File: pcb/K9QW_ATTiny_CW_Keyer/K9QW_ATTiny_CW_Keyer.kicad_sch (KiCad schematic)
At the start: 30 parts, among them J1 Paddle Input, J2 Key Output, J3 Command, J4 Sidetone, J5 Barrel_Jack_MountingPin, J6 Paddle Input, J7 Key Output, J8 LED, J9 Power Input, Q1 MMBT2222A, Q2 MMBT3904, Q3 MMBT3904, SW1 Command, SW2 Power Switch, U1 ATtiny85-20P, U2 LD1117S33TR_SOT223

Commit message: Rough PCB Layout
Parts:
- D1: value LED -> Key
- D2: value Side LED -> Sidetone
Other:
- moved on the sheet: R6
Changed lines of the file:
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@@
 	(wire
 		(pts
-			(xy 203.2 125.73) (xy 203.2 135.89)
+			(xy 205.74 125.73) (xy 205.74 135.89)
 		)
 		(stroke
@@
 	(wire
 		(pts
-			(xy 203.2 135.89) (xy 193.04 135.89)
+			(xy 205.74 135.89) (xy 193.04 135.89)
 		)
 		(stroke
@@
 	(wire
 		(pts
-			(xy 210.82 137.16) (xy 212.09 137.16)
+			(xy 212.09 137.16) (xy 214.63 137.16)
 		)
 		(stroke
@@
 	(wire
 		(pts
-			(xy 245.11 125.73) (xy 203.2 125.73)
+			(xy 245.11 125.73) (xy 205.74 125.73)
 		)
 		(stroke
@@
 	(wire
 		(pts
-			(xy 219.71 137.16) (xy 223.52 137.16)
+			(xy 222.25 137.16) (xy 223.52 137.16)
 		)
 		(stroke
@@
 			)
 		)
-		(property "Value" "LED"
+		(property "Value" "Key"
 			(at 196.85 132.3974 90)
 			(effects
@@
 	(symbol
 		(lib_id "power:VCC")
-		(at 210.82 137.16 90)
+		(at 212.09 137.16 90)
 		(unit 1)
 		(exclude_from_sim no)
@@
 		(dnp no)
 		(property "Reference" "#PWR020"
-			(at 214.63 137.16 0)
+			(at 215.9 137.16 0)
 			(effects
 				(font
@@
 		)
 		(property "Value" "VCC"
-			(at 205.74 137.16 0)
+			(at 207.01 137.16 0)
 			(effects
 				(font
@@
 		)
 		(property "Footprint" ""
-			(at 210.82 137.16 0)
+			(at 212.09 137.16 0)
 			(effects
 				(font
@@
 		)
 		(property "Datasheet" ""
-			(at 210.82 137.16 0)
+			(at 212.09 137.16 0)
 			(effects
 				(font
@@
 		)
 		(property "Description" "Power symbol creates a global label with name \"VCC\""
-			(at 210.82 137.16 0)
+			(at 212.09 137.16 0)
 			(effects
 				(font
@@
 			)
 		)
-		(property "Value" "Side LED"
+		(property "Value" "Sidetone"
 			(at 231.4575 133.35 0)
 			(effects
@@
 	(symbol
 		(lib_id "Device:R")
-		(at 215.9 137.16 270)
+		(at 218.44 137.16 270)
 		(unit 1)
 		(exclude_from_sim no)
@@
 		(fields_autoplaced yes)
 		(property "Reference" "R6"
-			(at 215.9 130.81 90)
+			(at 218.44 130.81 90)
 			(effects
 				(font
@@
 		)
 		(property "Value" "220"
-			(at 215.9 133.35 90)
+			(at 218.44 133.35 90)
 			(effects
 				(font
@@
 		)
 		(property "Footprint" "Resistor_SMD:R_0603_1608Metric_Pad0.98x0.95mm_HandSolder"
-			(at 215.9 135.382 90)
+			(at 218.44 135.382 90)
 			(effects
 				(font
@@
 		)
 		(property "Datasheet" "~"
-			(at 215.9 137.16 0)
+			(at 218.44 137.16 0)
 			(effects
 				(font
@@
 		)
 		(property "Description" "Resistor"
-			(at 215.9 137.16 0)
+			(at 218.44 137.16 0)
 			(effects
 				(font

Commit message: Layout cleanup
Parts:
- added JP1: SolderJumper_2_Open, Jumper:SolderJumper-2_P1.3mm_Open_RoundedPad1.0x1.5mm, symbol Jumper:SolderJumper_2_Open
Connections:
- net VCC: now also JP1.2 (B)
- net at C5.1, SW2.2 (B), U2.3 (VI): now also JP1.1 (A)
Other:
- moved on the sheet: C5, C6, SW2, U2

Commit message: Refining layout
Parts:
- added R7: 50, Resistor_SMD:R_0603_1608Metric_Pad0.98x0.95mm_HandSolder, symbol Device:R
- SW2: footprint Button_Switch_THT:SW_Slide-03_Wuerth-WS-SLTV_10x2.5x6.4_P2.54mm -> Connector_JST:JST_XH_B3B-XH-A_1x03_P2.50mm_Vertical
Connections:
- net DAH: now also J6.1 (Pin_1); no longer J6.2 (Pin_2)
- net DIT: now also J6.2 (Pin_2); no longer J6.3 (Pin_3)
- net GND: now also J6.3 (Pin_3), J7.3 (Pin_3), R7.2; no longer J6.1 (Pin_1), J7.1 (Pin_1), SW2.1 (A)
- net KEY Out: now also J7.2 (Pin_2); no longer J7.3 (Pin_3)
- net KEY Ring: now also J7.1 (Pin_1); no longer J7.2 (Pin_2)
- new net: R7.1, SW2.1 (A)
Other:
- moved on the sheet: J6, J7
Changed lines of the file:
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@@
 	(wire
 		(pts
-			(xy 240.03 24.13) (xy 242.57 24.13)
+			(xy 240.03 31.75) (xy 242.57 31.75)
 		)
 		(stroke
@@
 	(wire
 		(pts
+			(xy 54.61 86.36) (xy 55.88 86.36)
+		)
+		(stroke
+			(width 0)
+			(type default)
+		)
+	)
+	(wire
+		(pts
 			(xy 210.82 24.13) (xy 213.36 24.13)
 		)
@@
 	(wire
 		(pts
-			(xy 241.3 52.07) (xy 242.57 52.07)
+			(xy 241.3 59.69) (xy 242.57 59.69)
 		)
 		(stroke
@@
 	(wire
 		(pts
-			(xy 105.41 156.21) (xy 127 156.21)
+			(xy 63.5 86.36) (xy 64.77 86.36)
 		)
 		(stroke
@@
 	(wire
 		(pts
-			(xy 105.41 148.59) (xy 109.22 148.59)
+			(xy 105.41 156.21) (xy 127 156.21)
 		)
 		(stroke
@@
 	(wire
 		(pts
-			(xy 127 142.24) (xy 127 134.62)
+			(xy 105.41 148.59) (xy 109.22 148.59)
 		)
 		(stroke
@@
 	(wire
 		(pts
-			(xy 105.41 78.74) (xy 114.3 78.74)
+			(xy 127 142.24) (xy 127 134.62)
 		)
 		(stroke
@@
 	(wire
 		(pts
-			(xy 60.96 86.36) (xy 64.77 86.36)
+			(xy 105.41 78.74) (xy 114.3 78.74)
 		)
 		(stroke
@@
 		(on_board yes)
 		(dnp no)
-		(fields_autoplaced yes)
 		(property "Reference" "J3"
 			(at 232.41 81.2799 0)
@@
 	(symbol
 		(lib_id "Connector_Generic:Conn_01x03")
-		(at 247.65 54.61 0)
+		(at 247.65 57.15 0)
 		(unit 1)
 		(exclude_from_sim no)
@@
 		(fields_autoplaced yes)
 		(property "Reference" "J7"
-			(at 250.19 53.3399 0)
+			(at 250.19 55.8799 0)
 			(effects
 				(font
@@
 		)
 		(property "Value" "Key Output"
-			(at 250.19 55.8799 0)
+			(at 250.19 58.4199 0)
 			(effects
 				(font
@@
 		)
 		(property "Footprint" "Connector_JST:JST_XH_B3B-XH-A_1x03_P2.50mm_Vertical"
-			(at 247.65 54.61 0)
+			(at 247.65 57.15 0)
 			(effects
 				(font
@@
 		)
 		(property "Datasheet" "~"
-			(at 247.65 54.61 0)
+			(at 247.65 57.15 0)
 			(effects
 				(font
@@
 		)
 		(property "Description" "Generic connector, single row, 01x03, script generated (kicad-library-utils/schlib/autogen/connector/)"
-			(at 247.65 54.61 0)
+			(at 247.65 57.15 0)
 			(effects
 				(font
@@
 	(symbol
 		(lib_id "Connector_Generic:Conn_01x03")
-		(at 247.65 26.67 0)
+		(at 247.65 29.21 0)
 		(unit 1)
 		(exclude_from_sim no)
@@
 		(fields_autoplaced yes)
 		(property "Reference" "J6"
-			(at 250.19 25.3999 0)
+			(at 250.19 27.9399 0)
 			(effects
 				(font
@@
 		)
 		(property "Value" "Paddle Input"
-			(at 250.19 27.9399 0)
+			(at 250.19 30.4799 0)
 			(effects
 				(font
@@
 		)
 		(property "Footprint" "Connector_JST:JST_XH_B3B-XH-A_1x03_P2.50mm_Vertical"
-			(at 247.65 26.67 0)
+			(at 247.65 29.21 0)
 			(effects
 				(font
@@
 		)
 		(property "Datasheet" "~"
-			(at 247.65 26.67 0)
+			(at 247.65 29.21 0)
 			(effects
 				(font
@@
 		)
 		(property "Description" "Generic connector, single row, 01x03, script generated (kicad-library-utils/schlib/autogen/connector/)"
-			(at 247.65 26.67 0)
+			(at 247.65 29.21 0)
 			(effects
 				(font
@@
 	(symbol
 		(lib_id "power:GND")
-		(at 60.96 86.36 270)
+		(at 54.61 86.36 270)
 		(unit 1)
 		(exclude_from_sim no)
@@
 		(fields_autoplaced yes)
 		(property "Reference" "#PWR016"
-			(at 54.61 86.36 0)
+			(at 48.26 86.36 0)
 			(effects
 				(font
@@
 		)
 		(property "Value" "GND"
-			(at 57.15 86.3599 90)
+			(at 50.8 86.3599 90)
 			(effects
 				(font
@@
 		)
 		(property "Footprint" ""
-			(at 60.96 86.36 0)
+			(at 54.61 86.36 0)
 			(effects
 				(font
@@
 		)
 		(property "Datasheet" ""
-			(at 60.96 86.36 0)
+			(at 54.61 86.36 0)
 			(effects
 				(font
@@
 		)
 		(property "Description" "Power symbol creates a global label with name \"GND\" , ground"
-			(at 60.96 86.36 0)
+			(at 54.61 86.36 0)
 			(effects
 				(font
@@
 			)
 		)
-		(property "Footprint" "Button_Switch_THT:SW_Slide-03_Wuerth-WS-SLTV_10x2.5x6.4_P2.54mm"
+		(property "Footprint" "Connector_JST:JST_XH_B3B-XH-A_1x03_P2.50mm_Vertical"
 			(at 69.85 88.9 0)
 			(effects
@@
 	(symbol
 		(lib_id "power:GND")
-		(at 240.03 24.13 270)
+		(at 240.03 31.75 270)
 		(unit 1)
 		(exclude_from_sim no)
@@
 		(fields_autoplaced yes)
 		(property "Reference" "#PWR017"
-			(at 233.68 24.13 0)
+			(at 233.68 31.75 0)
 			(effects
 				(font
@@
 		)
 		(property "Value" "GND"
-			(at 236.22 24.1299 90)
+			(at 236.22 31.7499 90)
 			(effects
 				(font
@@
 		)
 		(property "Footprint" ""
-			(at 240.03 24.13 0)
+			(at 240.03 31.75 0)
 			(effects
 				(font
@@
 		)
 		(property "Datasheet" ""
-			(at 240.03 24.13 0)
+			(at 240.03 31.75 0)
 			(effects
 				(font
@@
 		)
 		(property "Description" "Power symbol creates a global label with name \"GND\" , ground"
-			(at 240.03 24.13 0)
+			(at 240.03 31.75 0)
 			(effects
 				(font
@@
 	(symbol
 		(lib_id "power:GND")
-		(at 241.3 52.07 270)
+		(at 241.3 59.69 270)
 		(unit 1)
 		(exclude_from_sim no)
@@
 		(fields_autoplaced yes)
 		(property "Reference" "#PWR018"
-			(at 234.95 52.07 0)
+			(at 234.95 59.69 0)
 			(effects
 				(font
@@
 		)
 		(property "Value" "GND"
-			(at 237.49 52.0699 90)
+			(at 237.49 59.6899 90)
 			(effects
 				(font
@@
 		)
 		(property "Footprint" ""
-			(at 241.3 52.07 0)
+			(at 241.3 59.69 0)
 			(effects
 				(font
@@
 		)
 		(property "Datasheet" ""
-			(at 241.3 52.07 0)
+			(at 241.3 59.69 0)
 			(effects
 				(font
@@
 		)
 		(property "Description" "Power symbol creates a global label with name \"GND\" , ground"
-			(at 241.3 52.07 0)
+			(at 241.3 59.69 0)
 			(effects
 				(font
@@
 	)
 	(symbol
+		(lib_id "Device:R")
+		(at 59.69 86.36 270)
+		(unit 1)
+		(exclude_from_sim no)
+		(in_bom yes)
+		(on_board yes)
+		(dnp no)
+		(fields_autoplaced yes)
+		(property "Reference" "R7"
+			(at 59.69 80.01 90)
+			(effects
+				(font
+					(size 1.27 1.27)
+				)
+			)
+		)
+		(property "Value" "50"
+			(at 59.69 82.55 90)
+			(effects
+				(font
+					(size 1.27 1.27)
+				)
+			)
+		)
+		(property "Footprint" "Resistor_SMD:R_0603_1608Metric_Pad0.98x0.95mm_HandSolder"
+			(at 59.69 84.582 90)
+			(effects
+				(font
+					(size 1.27 1.27)
+				)
+				(hide yes)
+			)
+		)
+		(property "Datasheet" "~"
+			(at 59.69 86.36 0)
+			(effects
+				(font
+					(size 1.27 1.27)
+				)
+				(hide yes)
+			)
+		)
+		(property "Description" "Resistor"
+			(at 59.69 86.36 0)
+			(effects
+				(font
+					(size 1.27 1.27)
+				)
+				(hide yes)
+			)
+		)
+		(pin "1"
+		)
+		(pin "2"
+		)
+		(instances
+			(project "K9QW_ATTiny_CW_Keyer"
+				(path "/aef77cdf-c6ea-4cd5-9717-5394839cbff2"
+					(reference "R7")
+					(unit 1)
+				)
+			)
+		)
+	)
+	(symbol
 		(lib_id "Connector_Generic:Conn_01x02")
 		(at 229.87 106.68 0)
@@
 		(on_board yes)
 		(dnp no)
-		(fields_autoplaced yes)
 		(property "Reference" "J4"
 			(at 232.41 106.6799 0)

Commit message: Refining routing
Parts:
- added J10: Mounting Hole, MountingHole:MountingHole_3.2mm_M3_Pad_TopBottom, symbol Connector:Conn_01x01_Pin
- added JP2: Bypass Switch, Jumper:SolderJumper-2_P1.3mm_Open_RoundedPad1.0x1.5mm, symbol Jumper:SolderJumper_2_Open
- JP1: value SolderJumper_2_Open -> Bypass Regulator
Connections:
- net GND: now also C4.2, Q1.2 (E), J10.1 (Pin_1)
- net VDC: now also JP2.2 (B)
- net at C5.1, JP1.1 (A), SW2.2 (B)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: now also JP2.1 (A)

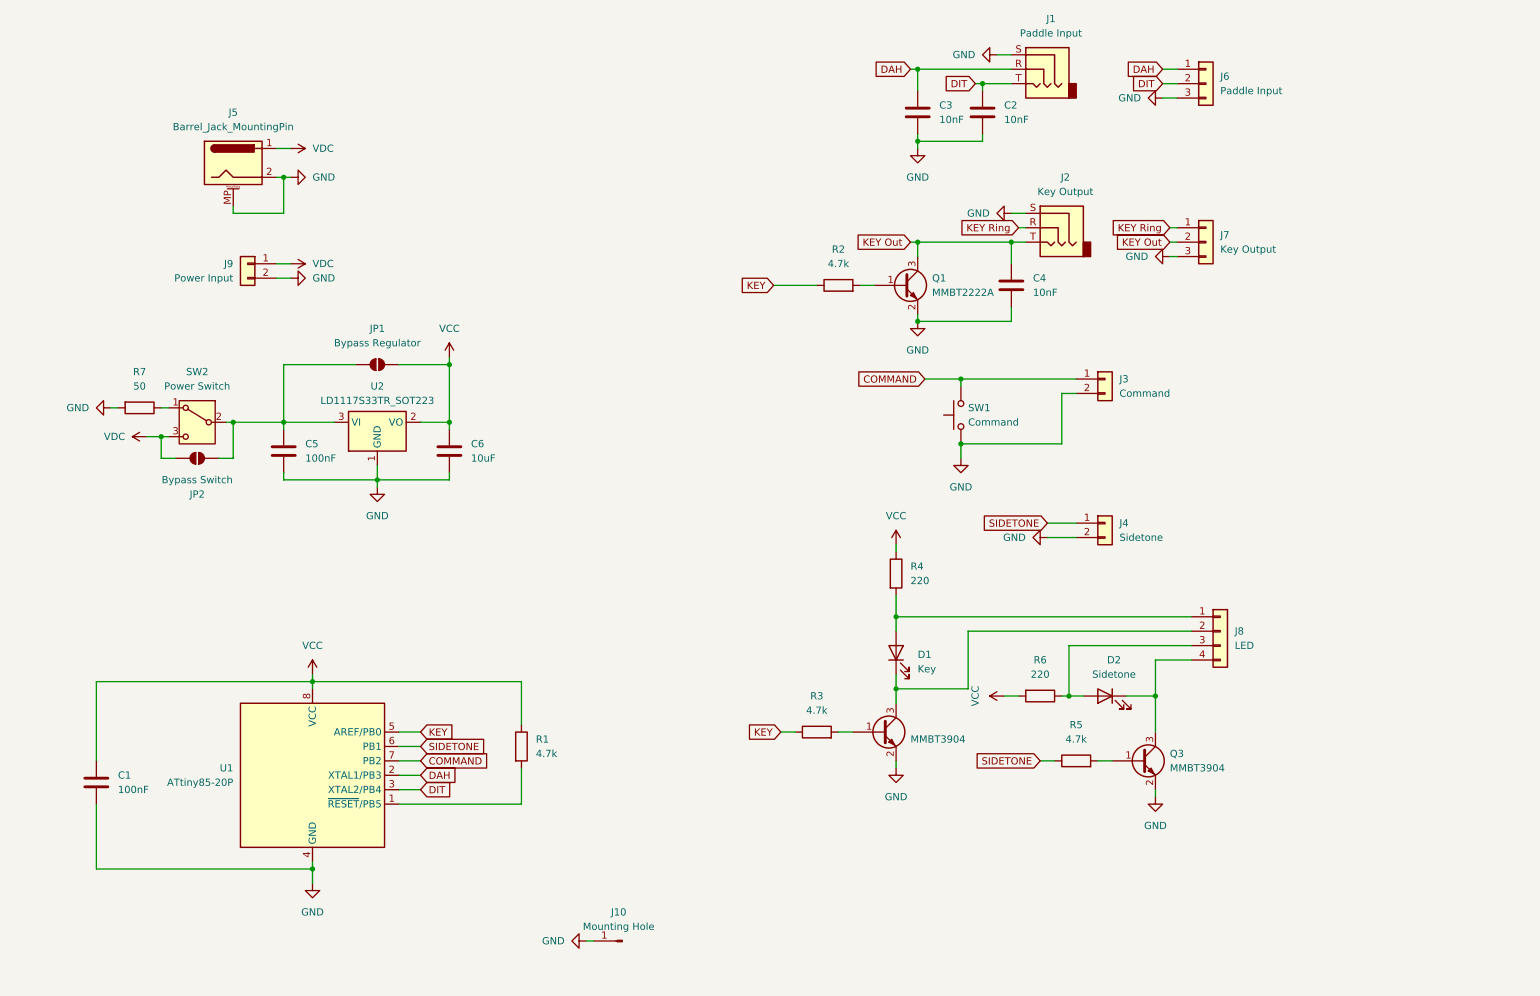
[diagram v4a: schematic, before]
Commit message: Stripping panel mount headers
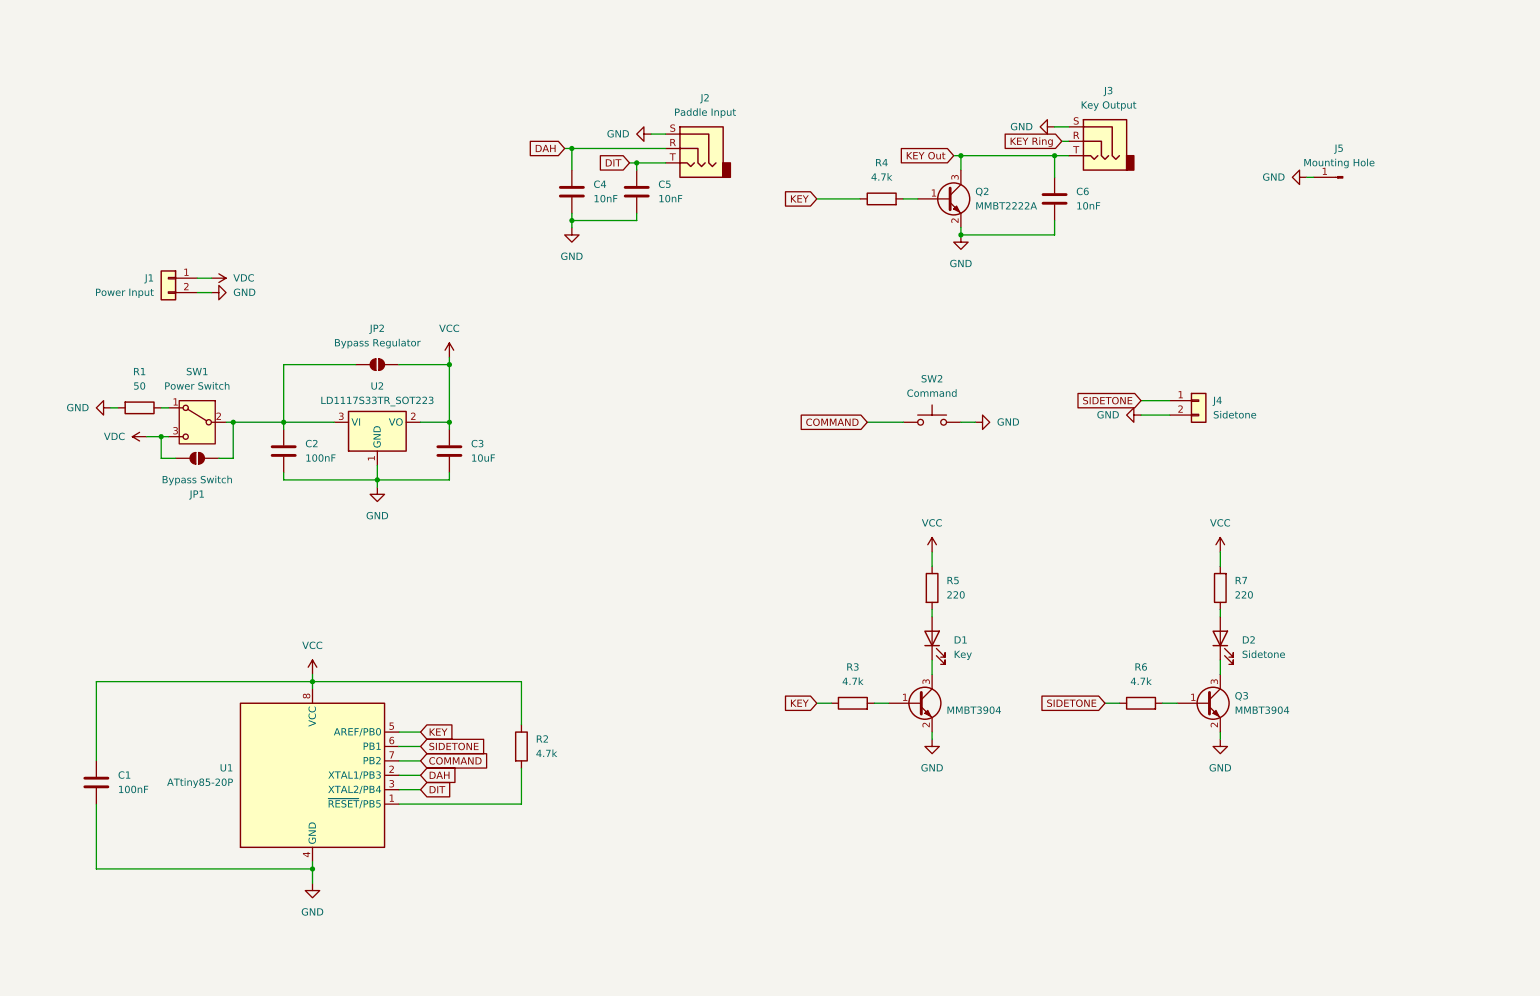
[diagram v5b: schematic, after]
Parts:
- removed J3: Command, Connector_JST:JST_XH_B2B-XH-A_1x02_P2.50mm_Vertical, symbol Connector_Generic:Conn_01x02
- removed J5: Barrel_Jack_MountingPin, Connector_BarrelJack:BarrelJack_CUI_PJ-063AH_Horizontal, symbol Connector:Barrel_Jack_MountingPin
- removed J6: Paddle Input, Connector_JST:JST_XH_B3B-XH-A_1x03_P2.50mm_Vertical, symbol Connector_Generic:Conn_01x03
- removed J7: Key Output, Connector_JST:JST_XH_B3B-XH-A_1x03_P2.50mm_Vertical, symbol Connector_Generic:Conn_01x03
- removed J8: LED, Connector_JST:JST_XH_B4B-XH-A_1x04_P2.50mm_Vertical, symbol Connector_Generic:Conn_01x04
- renumbered C5 to C2, C6 to C3, C3 to C4, C2 to C5, C4 to C6, J9 to J1, J1 to J2, J2 to J3, J10 to J5, JP2 to JP1, JP1 to JP2, Q2 to Q1, Q1 to Q2, R7 to R1, R1 to R2, R2 to R4, R4 to R5, R5 to R6, R6 to R7, SW2 to SW1, SW1 to SW2
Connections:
- net COMMAND: now also SW2.1; no longer SW2.2
- net GND: now also SW2.2; no longer SW2.1
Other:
- moved on the sheet: C4, C5, C6, D1, J1, J2, J3, J4, J5, Q2, Q3, R3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

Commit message: Removed panel headers, added reverse polarity protection, rough layout
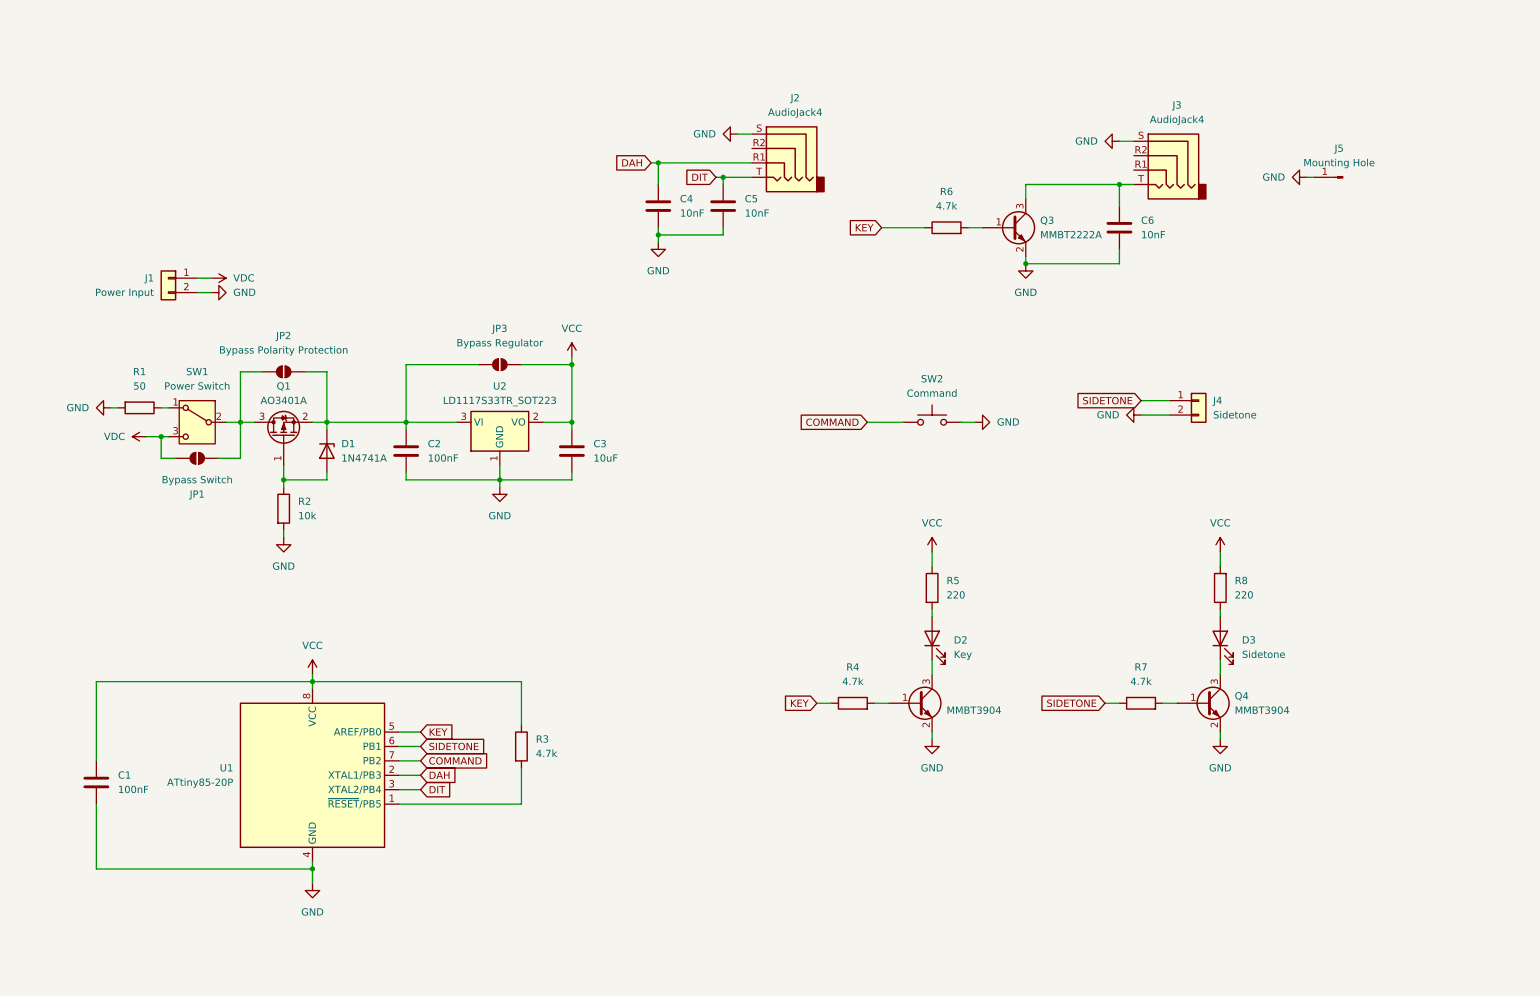
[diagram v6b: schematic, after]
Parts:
- removed J2: Paddle Input, Connector_Audio:Jack_3.5mm_CUI_SJ1-3523N_Horizontal, symbol Connector_Audio:AudioJack3
- removed J3: Key Output, Connector_Audio:Jack_3.5mm_CUI_SJ1-3523N_Horizontal, symbol Connector_Audio:AudioJack3
- added D1: 1N4741A, Diode_THT:D_DO-41_SOD81_P10.16mm_Horizontal, symbol Diode:1N47xxA
- added J2, J3: AudioJack4, Connector_Audio:Jack_3.5mm_PJ320D_Horizontal, symbol Connector_Audio:AudioJack4
- added JP2: Bypass Polarity Protection, Jumper:SolderJumper-2_P1.3mm_Open_RoundedPad1.0x1.5mm, symbol Jumper:SolderJumper_2_Open
- added Q1: AO3401A, Package_TO_SOT_SMD:SOT-23, symbol Transistor_FET:AO3401A
- added R2: 10k, Resistor_SMD:R_0603_1608Metric_Pad0.98x0.95mm_HandSolder, symbol Device:R
- renumbered D1 to D2, D2 to D3, JP2 to JP3, Q1 to Q2, Q2 to Q3, Q3 to Q4, R2 to R3, R3 to R4, R4 to R6, R6 to R7, R7 to R8
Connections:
- net DAH: now also J2.R1
- net DIT: now also J2.T
- net GND: now also J2.S, J3.S, R2.2
- net at C2.1, JP3.1 (A), U2.3 (VI): now also D1.1 (K), JP2.2 (B), Q1.2 (S); no longer JP1.1 (A), SW1.2 (B)
- net KEY Out: no longer names the net of C6.1, Q3.3 (C)
- net KEY Out: now also J3.T
- new net: JP1.1 (A), JP2.1 (A), Q1.3 (D), SW1.2 (B)
- new net: D1.2 (A), Q1.1 (G), R2.1
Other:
- moved on the sheet: C2, C3, C4, C5, C6, JP3, Q3, R6, U2
